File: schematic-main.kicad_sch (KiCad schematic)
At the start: 12 parts, among them J1 Fell_Cell_IN, J2 CAN, J3 P_Valve, J4 FC Cooling, J5 Valve, J7 Axilary_Out, J9 Analog_In, P1 USB_C_Plug_USB2.0

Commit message: Repair files
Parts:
- removed J3: P_Valve, Connector_Molex:Molex_Mini-Fit_Jr_5569-02A2_2x01_P4.20mm_Horizontal, symbol Connector_Generic:Conn_01x02
- removed J4: FC Cooling, Connector_Molex:Molex_Mini-Fit_Jr_5569-10A1_2x05_P4.20mm_Horizontal, symbol Connector_Generic:Conn_02x05_Top_Bottom
- removed J5: Valve, Connector_Molex:Molex_Mini-Fit_Jr_5569-02A2_2x01_P4.20mm_Horizontal, symbol Connector_Generic:Conn_01x02
- removed J7: Axilary_Out, Connector_Molex:Molex_Mini-Fit_Jr_5569-02A2_2x01_P4.20mm_Horizontal, symbol Connector_Generic:Conn_01x02
- removed J9: Analog_In, Connector_Molex:Molex_Mini-Fit_Jr_5569-02A2_2x01_P4.20mm_Horizontal, symbol Connector_Generic:Conn_01x02
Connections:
- net IO/CANH: no longer names the net of J2.1 (Pin_1)
- net IO/CANL: no longer names the net of J2.2 (Pin_2)
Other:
- sheet Step Down Converter renamed Converter
- sheet Converter ports: added 12V, 3.3V, 5V, Converter_ON, Converter_PWM, FC+, FC_V, FC_c, GND, MC+, MC_c, SC+, SC_V, SC_c; removed none
- sheet IO ports: added none; removed 12V, 3.3V, A_Input, Analog_MCU, CANH, CANL, CAN_RX, CAN_TX, FAN_1_TACHO, FAN_1_TACHO_MCU, FAN_2_TACHO, FAN_2_TACHO_MCU, FAN_GND, FAN_ON_MCU, FAN_PWM, FAN_PWM_MCU, FC_Voltage_MCU, GND, LED_CAN_STATUS, LED_MCU_STATUS, Main_Valve, Main_Valve_MCU, PURGE_VALVE, PURGE_VALVE_MCU, SC_V, Temp_MCU, Temp_sensor, out_12V
- sheet MCU ports: added none; removed FAN_1_TACHO_MCU, FAN_2_TACHO_MCU, FAN_ON_MCU, FAN_PWM_MCU, Main_Valve_MCU, PURGE_VALVE_MCU

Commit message: P1
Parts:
- J1: value Fell_Cell_IN -> Battery
- J2: symbol Connector_Generic:Conn_01x02 -> Connector_Generic:Conn_01x03
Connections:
- net GND: now also J2.3 (Pin_3)
- net IO/CANH: now reaches J2.1 (Pin_1)
- net IO/CANL: now reaches J2.2 (Pin_2)
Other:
- sheet IO ports: added CANH, CANL; removed none
- sheet Power  ports: added none; removed SC_V
- note added: "10-16,8V"
- note removed: "30-62V"
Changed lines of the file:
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@@
-    (stroke (width 0) (type default))
-  )
-  (wire (pts (xy 56.007 114.7826) (xy 56.007 114.808))
     (stroke (width 0) (type default))
   )
@@
     (stroke (width 0) (type default))
   )
-  (wire (pts (xy 126.492 119.634) (xy 134.62 119.634))
+  (wire (pts (xy 125.73 121.92) (xy 134.62 121.92))
     (stroke (width 0) (type default))
   )
@@
     (stroke (width 0) (type default))
   )
-  (wire (pts (xy 56.007 114.808) (xy 134.62 114.8334))
-    (stroke (width 0) (type default))
-  )
   (wire (pts (xy 73.66 107.95) (xy 134.62 107.95))
     (stroke (width 0) (type default))
@@
     (stroke (width 0) (type default))
   )
-  (wire (pts (xy 126.492 122.174) (xy 134.62 122.174))
-    (stroke (width 0) (type default))
-  )
   (wire (pts (xy 66.04 33.02) (xy 73.66 33.02))
     (stroke (width 0) (type default))
@@
     (stroke (width 0) (type default))
   )
-  (wire (pts (xy 56.007 114.7826) (xy 56.0832 114.7826))
+  (wire (pts (xy 125.73 124.46) (xy 134.62 124.46))
     (stroke (width 0) (type default))
   )
@@
     (stroke (width 0) (type default))
   )
-  (wire (pts (xy 56.0832 114.7826) (xy 56.0832 39.37))
-    (stroke (width 0) (type default))
-  )
   (wire (pts (xy 120.65 54.61) (xy 134.62 54.61))
     (stroke (width 0) (type default))
@@
     (stroke (width 0) (type default))
   )
-  (text "30-62V" (at 21.59 35.56 90)
+  (text "10-16,8V" (at 21.59 35.56 90)
     (effects (font (size 1.27 1.27) (thickness 0.254) bold) (justify left bottom))
   )
@@
     (effects (font (size 1.27 1.27)) (justify right bottom))
   )
-  (symbol (lib_id "power:GND") (at 125.73 141.605 0) (unit 1)
-    (in_bom yes) (on_board yes) (dnp no) (fields_autoplaced)
-    (property "Reference" "#PWR04" (at 125.73 147.955 0)
-      (effects (font (size 1.27 1.27)) hide)
-    )
-    (property "Value" "GND" (at 125.73 146.685 0)
-      (effects (font (size 1.27 1.27)) hide)
-    )
-    (property "Footprint" "" (at 125.73 141.605 0)
-      (effects (font (size 1.27 1.27)) hide)
-    )
-    (property "Datasheet" "" (at 125.73 141.605 0)
+  (symbol (lib_id "power:GND") (at 125.73 127 0) (unit 1)
+    (in_bom yes) (on_board yes) (dnp no) (fields_autoplaced)
+    (property "Reference" "#PWR04" (at 125.73 133.35 0)
+      (effects (font (size 1.27 1.27)) hide)
+    )
+    (property "Value" "GND" (at 125.73 132.08 0)
+      (effects (font (size 1.27 1.27)) hide)
+    )
+    (property "Footprint" "" (at 125.73 127 0)
+      (effects (font (size 1.27 1.27)) hide)
+    )
+    (property "Datasheet" "" (at 125.73 127 0)
       (effects (font (size 1.27 1.27)) hide)
     )
@@
     )
   )
-  (symbol (lib_id "Connector_Generic:Conn_01x02") (at 121.412 119.634 0) (mirror y) (unit 1)
+  (symbol (lib_id "Connector_Generic:Conn_01x03") (at 120.65 124.46 0) (mirror y) (unit 1)
     (in_bom yes) (on_board yes) (dnp no)
-    (property "Reference" "J2" (at 118.872 119.634 0)
-      (effects (font (size 1.27 1.27)) (justify left))
-    )
-    (property "Value" "CAN" (at 118.872 122.174 0)
-      (effects (font (size 1.27 1.27)) (justify left))
-    )
-    (property "Footprint" "Connector_Molex:Molex_Mini-Fit_Jr_5569-02A2_2x01_P4.20mm_Horizontal" (at 121.412 119.634 0)
-      (effects (font (size 1.27 1.27)) hide)
-    )
-    (property "Datasheet" "~" (at 121.412 119.634 0)
+    (property "Reference" "J2" (at 118.11 124.46 0)
+      (effects (font (size 1.27 1.27)) (justify left))
+    )
+    (property "Value" "CAN" (at 118.11 127 0)
+      (effects (font (size 1.27 1.27)) (justify left))
+    )
+    (property "Footprint" "Connector_Molex:Molex_Mini-Fit_Jr_5569-02A2_2x01_P4.20mm_Horizontal" (at 120.65 124.46 0)
+      (effects (font (size 1.27 1.27)) hide)
+    )
+    (property "Datasheet" "~" (at 120.65 124.46 0)
       (effects (font (size 1.27 1.27)) hide)
     )
     (pin "1")
     (pin "2")
+    (pin "3")
     (instances
       (project "schematic-main"
@@
       (effects (font (size 1.27 1.27)))
     )
-    (property "Value" "Fell_Cell_IN" (at 17.78 31.75 90)
+    (property "Value" "Battery" (at 17.78 31.75 90)
       (effects (font (size 1.27 1.27)))
     )
@@
       (effects (font (size 1.27 1.27)) (justify left top) hide)
     )
+    (pin "CANL" bidirectional (at 134.62 124.46 180)
+      (effects (font (size 1.27 1.27)) (justify left))
+    )
+    (pin "CANH" bidirectional (at 134.62 121.92 180)
+      (effects (font (size 1.27 1.27)) (justify left))
+    )
     (instances
       (project "schematic-main"
@@
       (effects (font (size 1.27 1.27)) (justify left))
     )
-    (pin "SC_V" output (at 56.0832 39.37 270)
-      (effects (font (size 1.27 1.27)) (justify left))
-    )

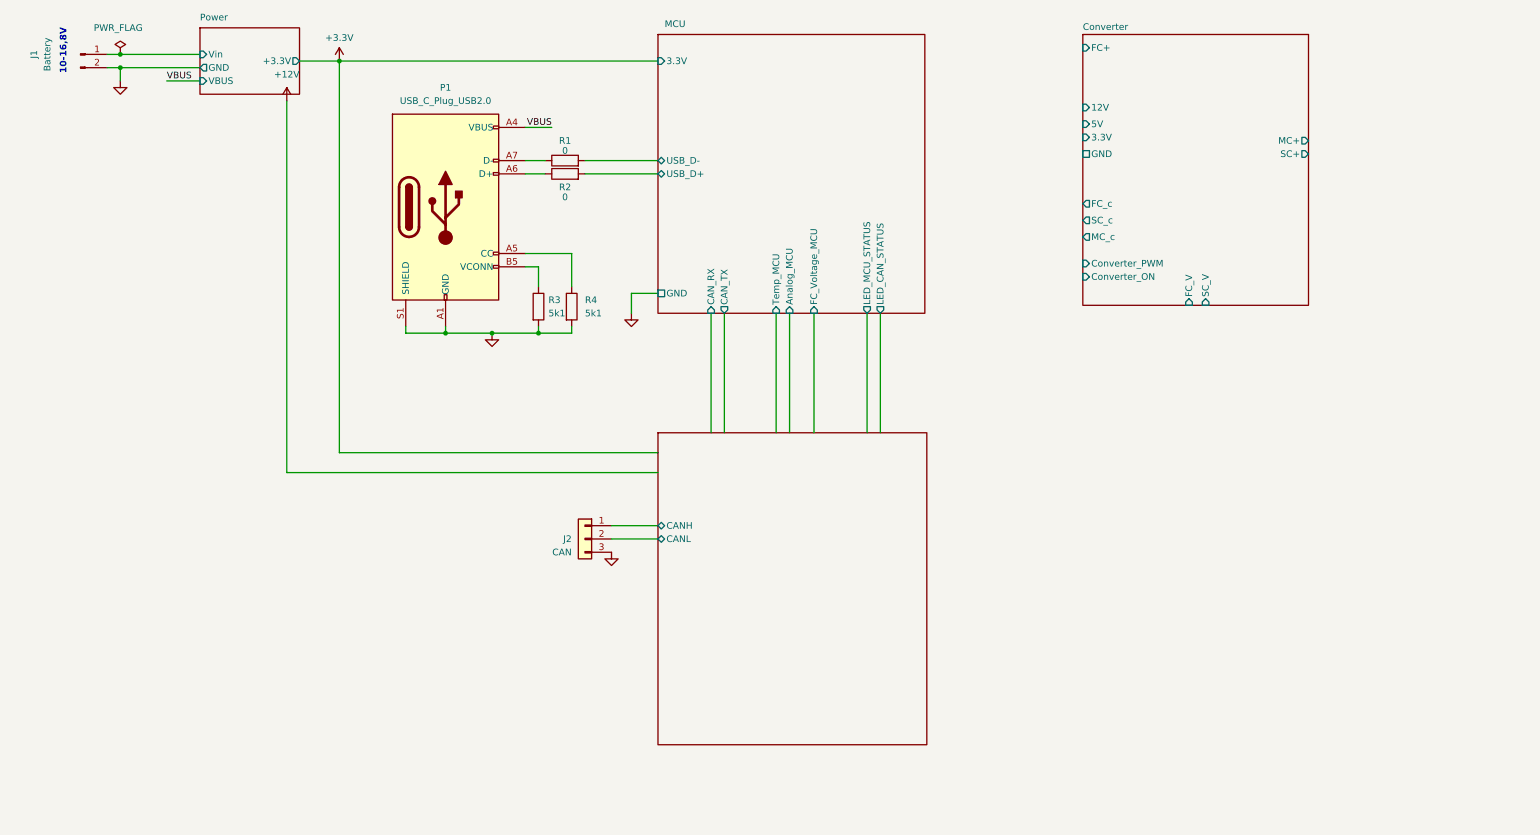
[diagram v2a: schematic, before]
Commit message: Edit mosfets outputs
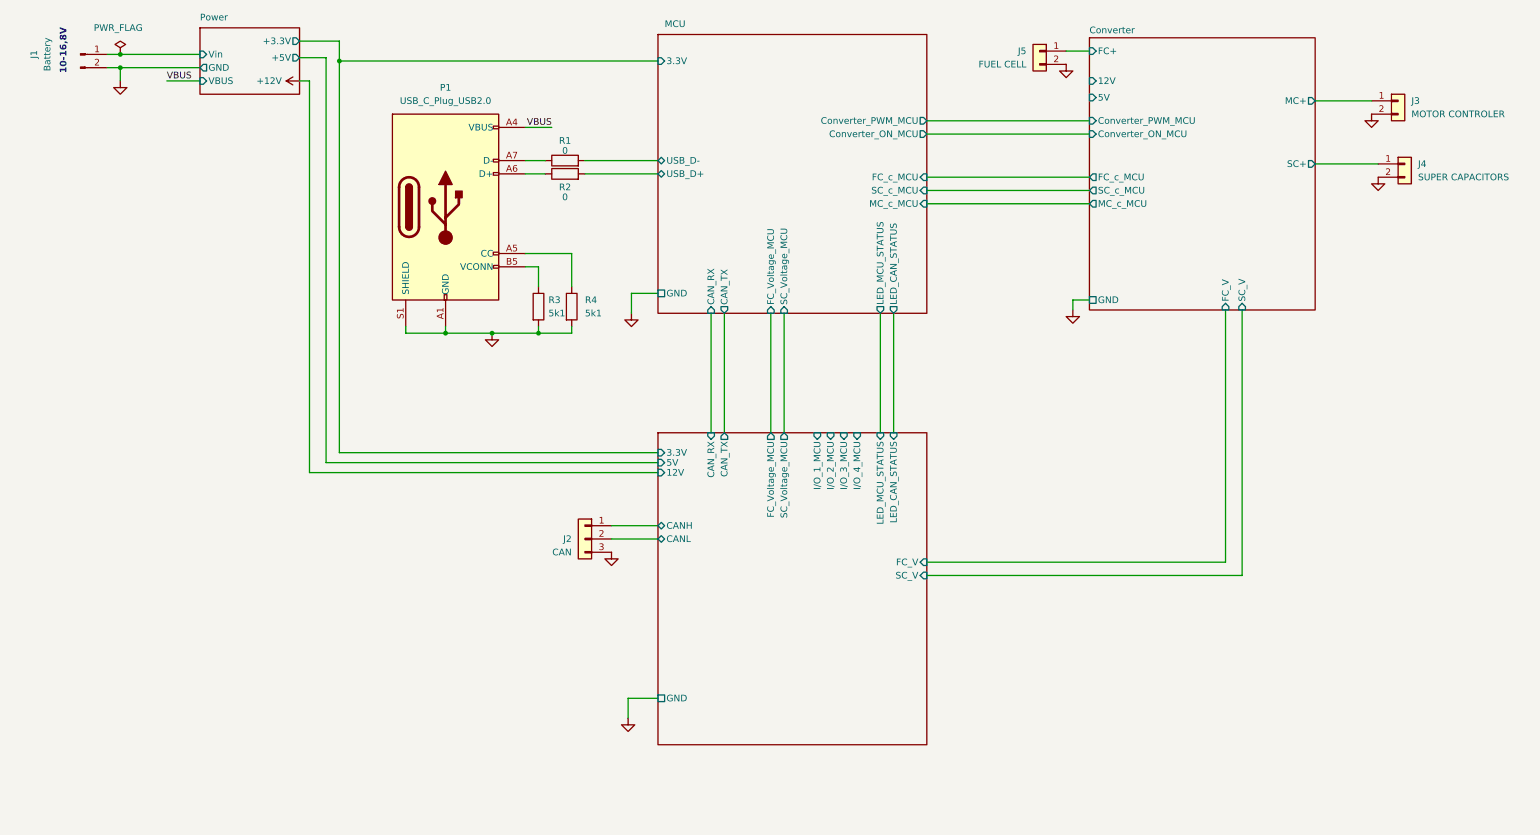
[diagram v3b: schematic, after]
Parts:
- added J3: MOTOR CONTROLER, Connector_Molex:Molex_Mini-Fit_Jr_5569-02A2_2x01_P4.20mm_Horizontal, symbol Connector_Generic:Conn_01x02
- added J4: SUPER CAPACITORS, Connector_Molex:Molex_Mini-Fit_Jr_5569-02A2_2x01_P4.20mm_Horizontal, symbol Connector_Generic:Conn_01x02
- added J5: FUEL CELL, library:XT30PWF, symbol Connector_Generic:Conn_01x02
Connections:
- net Converter/FC+: now also J5.1 (Pin_1)
- net Converter/MC+: now also J3.1 (Pin_1)
- net Converter/SC+: now also J4.1 (Pin_1)
- net GND: now also J3.2 (Pin_2), J4.2 (Pin_2), J5.2 (Pin_2)
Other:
- sheet Converter ports: added Converter_ON_MCU, Converter_PWM_MCU, FC_c_MCU, MC_c_MCU, SC_c_MCU; removed 3.3V, Converter_ON, Converter_PWM, FC_c, MC_c, SC_c
- sheet IO ports: added 12V, 3.3V, 5V, CAN_RX, CAN_TX, FC_V, FC_Voltage_MCU, GND, I/O_1_MCU, I/O_2_MCU, I/O_3_MCU, I/O_4_MCU, LED_CAN_STATUS, LED_MCU_STATUS, SC_V, SC_Voltage_MCU; removed none
- sheet MCU ports: added Converter_ON_MCU, Converter_PWM_MCU, FC_c_MCU, MC_c_MCU, SC_Voltage_MCU, SC_c_MCU; removed Analog_MCU, Temp_MCU
- sheet Power  ports: added +5V; removed none

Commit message: First pcb
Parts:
- added J4: Joulemeter, Connector_Molex:Molex_Mini-Fit_Jr_5569-02A2_2x01_P4.20mm_Horizontal, symbol Connector_Generic:Conn_01x02
- J1: value Battery -> Battery converter
- J2: footprint Connector_Molex:Molex_Mini-Fit_Jr_5569-02A2_2x01_P4.20mm_Horizontal -> Lib:39303035
- J5: renamed from J3; footprint Connector_Molex:Molex_Mini-Fit_Jr_5569-02A2_2x01_P4.20mm_Horizontal -> library:XT60PWM
- J6: renamed from J4; footprint Connector_Molex:Molex_Mini-Fit_Jr_5569-02A2_2x01_P4.20mm_Horizontal -> library:XT60PWM
- renumbered J5 to J3, R3 to R1, R1 to R2, R2 to R3
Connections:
- net GND: now also J1.1 (Pin_1), J4.2 (Pin_2); no longer J1.2 (Pin_2)
- net Power /Vin: now also J1.2 (Pin_2); no longer J1.1 (Pin_1)
- new net Converter/jSC+: J4.1 (Pin_1)
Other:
- sheet Converter ports: added jSC+; removed none
- sheet MCU ports: added I/O_1_MCU, I/O_2_MCU, I/O_3_MCU, I/O_4_MCU; removed none
- note added: "12V"
- note removed: "10-16,8V"
- moved on the sheet: J3, J5, J6

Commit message: Buck - boost converter
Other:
- sheet Converter ports: added Converter_ON_A_MCU, Converter_ON_B_MCU, Converter_PWM_A_MCU, Converter_PWM_B_MCU; removed Converter_ON_MCU, Converter_PWM_MCU
- sheet MCU ports: added Converter_ON_A_MCU, Converter_ON_B_MCU, Converter_PWM_A_MCU, Converter_PWM_B_MCU; removed Converter_ON_MCU, Converter_PWM_MCU
- moved on the sheet: J3

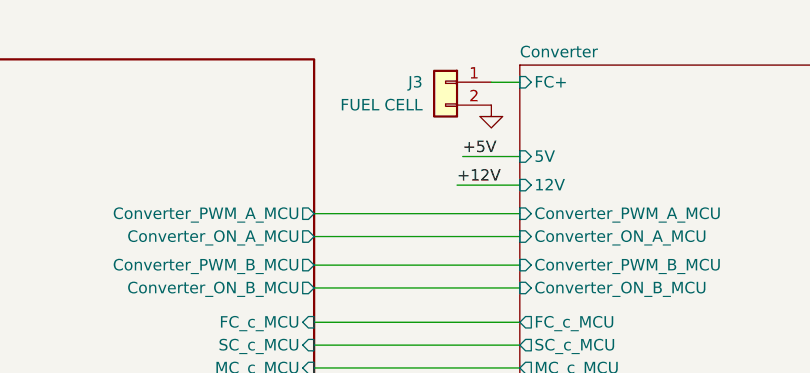
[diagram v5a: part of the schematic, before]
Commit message: Add coil and microcontroler
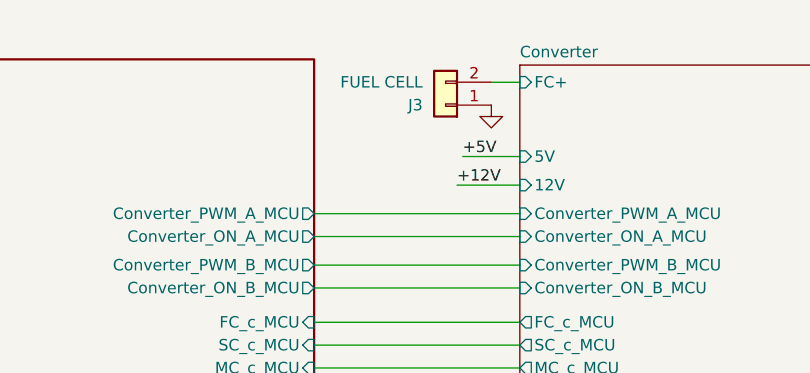
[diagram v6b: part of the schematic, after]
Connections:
- net Converter/FC+: now also J3.2 (Pin_2); no longer J3.1 (Pin_1)
- net GND: now also J3.1 (Pin_1); no longer J3.2 (Pin_2)
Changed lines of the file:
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@@
-	(symbol
-		(lib_id "Connector_Generic:Conn_01x02")
-		(at 200.66 30.48 0)
-		(mirror y)
-		(unit 1)
-		(exclude_from_sim no)
-		(in_bom yes)
-		(on_board yes)
-		(dnp no)
-		(property "Reference" "J3"
-			(at 198.12 30.48 0)
-			(effects
-				(font
-					(size 1.27 1.27)
-				)
-				(justify left)
-			)
-		)
-		(property "Value" "FUEL CELL"
-			(at 198.12 33.02 0)
-			(effects
-				(font
-					(size 1.27 1.27)
-				)
-				(justify left)
-			)
-		)
-		(property "Footprint" "library:XT30PWF"
-			(at 200.66 30.48 0)
-			(effects
-				(font
-					(size 1.27 1.27)
-				)
-				(hide yes)
-			)
-		)
-		(property "Datasheet" "~"
-			(at 200.66 30.48 0)
-			(effects
-				(font
-					(size 1.27 1.27)
-				)
-				(hide yes)
-			)
-		)
-		(property "Description" ""
-			(at 200.66 30.48 0)
-			(effects
-				(font
-					(size 1.27 1.27)
-				)
-				(hide yes)
-			)
-		)
-		(pin "1"
-		)
-		(pin "2"
-		)
-		(instances
-			(project "schematic-main"
-				(path "/c9ad7189-d3b2-414a-9743-efd8e57cd755"
-					(reference "J3")
-					(unit 1)
-				)
-			)
-		)
-	)
 	(symbol
 		(lib_id "Connector_Generic:Conn_01x02")
@@
 					(unit 1)
 				)
+			)
+		)
+	)
+	(symbol
+		(lib_id "Connector_Generic:Conn_01x02")
+		(at 200.66 33.02 180)
+		(unit 1)
+		(exclude_from_sim no)
+		(in_bom yes)
+		(on_board yes)
+		(dnp no)
+		(property "Reference" "J3"
+			(at 198.12 33.02 0)
+			(effects
+				(font
+					(size 1.27 1.27)
+				)
+				(justify left)
+			)
+		)
+		(property "Value" "FUEL CELL"
+			(at 198.12 30.48 0)
+			(effects
+				(font
+					(size 1.27 1.27)
+				)
+				(justify left)
+			)
+		)
+		(property "Footprint" "library:XT30PWF"
+			(at 200.66 33.02 0)
+			(effects
+				(font
+					(size 1.27 1.27)
+				)
+				(hide yes)
+			)
+		)
+		(property "Datasheet" "~"
+			(at 200.66 33.02 0)
+			(effects
+				(font
+					(size 1.27 1.27)
+				)
+				(hide yes)
+			)
+		)
+		(property "Description" ""
+			(at 200.66 33.02 0)
+			(effects
+				(font
+					(size 1.27 1.27)
+				)
+				(hide yes)
+			)
+		)
+		(pin "1"
+		)
+		(pin "2"
+		)
+		(instances
+			(project "schematic-main"
+				(path "/c9ad7189-d3b2-414a-9743-efd8e57cd755"
+					(reference "J3")
+					(unit 1)
+				)

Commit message: Add pot
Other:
- sheet IO ports: added SCL_D_Pot_i2c_MCU, SDA_D_Pot_i2c_MCU; removed none
- sheet MCU ports: added SCL_D_Pot_i2c_MCU, SDA_D_Pot_i2c_MCU; removed none
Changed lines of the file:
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@@
+	(wire
+		(pts
+			(xy 152.908 81.28) (xy 152.908 104.14)
+		)
+		(stroke
+			(width 0)
+			(type default)
+		)
+	)
 	(wire
 		(pts
@@
 		(pts
 			(xy 144.78 81.28) (xy 144.78 104.14)
+		)
+		(stroke
+			(width 0)
+			(type default)
+		)
+	)
+	(wire
+		(pts
+			(xy 150.495 81.28) (xy 150.495 104.14)
 		)
 		(stroke
@@
 			)
 		)
+		(pin "SDA_D_Pot_i2c_MCU" output
+			(at 152.908 104.14 90)
+			(effects
+				(font
+					(size 1.27 1.27)
+				)
+				(justify right)
+			)
+		)
+		(pin "SCL_D_Pot_i2c_MCU" output
+			(at 150.495 104.14 90)
+			(effects
+				(font
+					(size 1.27 1.27)
+				)
+				(justify right)
+			)
+		)
 		(instances
 			(project "schematic-main"
@@
 			)
 		)
+		(pin "SCL_D_Pot_i2c_MCU" output
+			(at 150.495 81.28 270)
+			(effects
+				(font
+					(size 1.27 1.27)
+				)
+				(justify left)
+			)
+		)
+		(pin "SDA_D_Pot_i2c_MCU" output
+			(at 152.908 81.28 270)
+			(effects
+				(font
+					(size 1.27 1.27)
+				)
+				(justify left)
+			)
+		)
